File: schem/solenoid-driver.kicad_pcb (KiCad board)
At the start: 2 copper layers, 45.2 x 21.2 mm, 21 parts, among them P1 CONN_3X2, P3 CONN_2, P4 Chassis GND, U1 MIC2009A-1, U2 ULN2003, U3 MIC2250-2

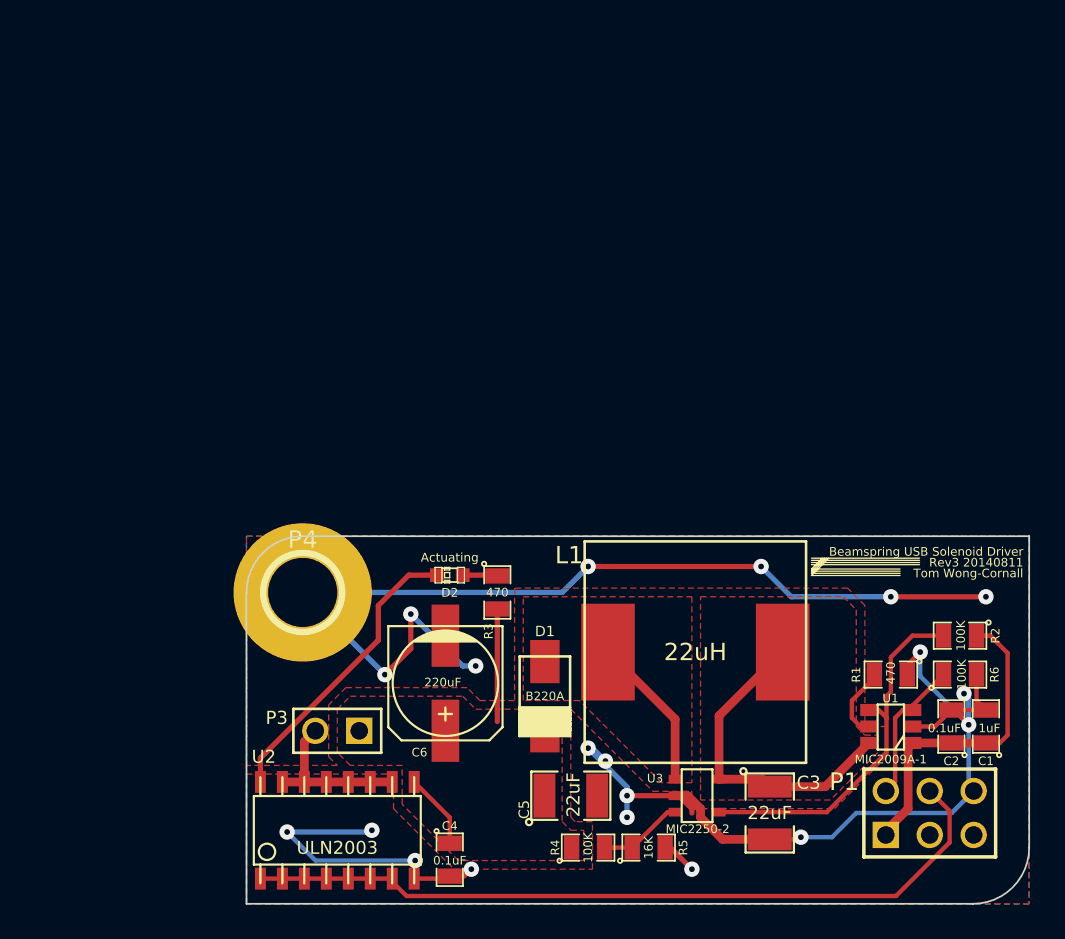
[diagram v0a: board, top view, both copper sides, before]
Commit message: Route the PCB
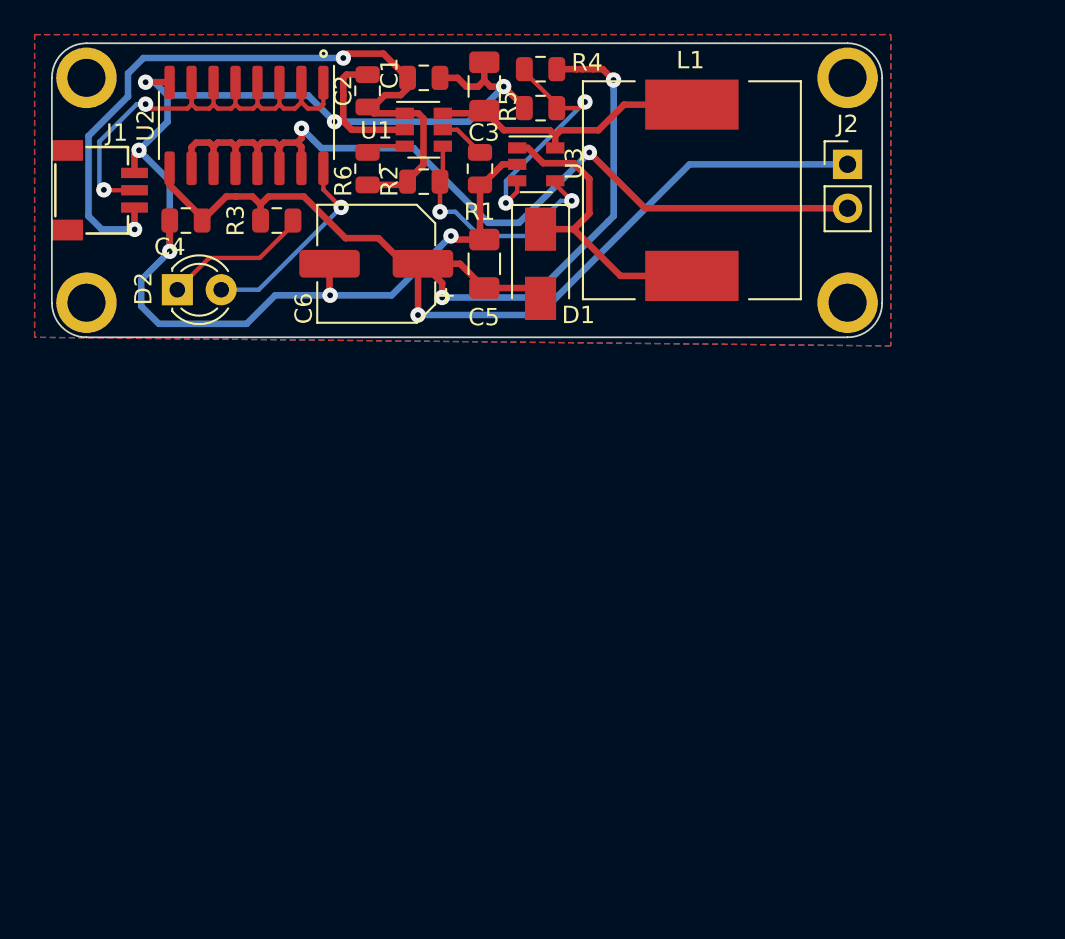
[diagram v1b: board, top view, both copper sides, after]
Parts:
- removed P1: CONN_3X2, pin_array_3x2
- removed P3: CONN_2, PIN_ARRAY_2X1
- removed P4: Chassis GND, 1pin
- added J1: Conn_01x03, random-keyboard-parts:JST-SR-3, F.Cu at (164.0, 117.5)
- added J2: SOLENOID, Connector_PinHeader_2.54mm:PinHeader_1x02_P2.54mm_Vertical, F.Cu at (210.0, 116.0)
- added MH1: Conn_01x01, random-keyboard-parts:Generic-Mounthole, F.Cu at (166.0, 111.0)
- added MH2: Conn_01x01, random-keyboard-parts:Generic-Mounthole, F.Cu at (166.0, 124.0)
- added MH3: Conn_01x01, random-keyboard-parts:Generic-Mounthole, F.Cu at (210.0, 111.0)
- added MH4: Conn_01x01, random-keyboard-parts:Generic-Mounthole, F.Cu at (210.0, 124.0)
- C1, C2, C4: footprint SM0805 -> Capacitor_SMD:C_0805_2012Metric
- C3, C5: footprint SM1210 -> Capacitor_SMD:C_1206_3216Metric
- C6: footprint c_elec_6.3x7.7 -> Capacitor_SMD:CP_Elec_6.3x7.7
- D1: footprint DO214AC_SMA -> Diode_SMD:D_SMA
- D2: footprint LED-0603 -> LED_THT:LED_D3.0mm
- L1: footprint INDUCTOR_12.8x12.8 -> Inductor_SMD:L_12x12mm_H6mm
- R1, R2, R3, R4, R5, R6: footprint SM0805 -> Resistor_SMD:R_0805_2012Metric
- U1: footprint SOT23_6 -> Package_TO_SOT_SMD:SOT-23-6
- U2: footprint so-16 -> Package_SO:SOIC-16_3.9x9.9mm_P1.27mm
- U3: footprint SOT23-5 -> Package_TO_SOT_SMD:SOT-23-5
- moved C2 49.9 mm to (182.2, 111.8)
- moved C1 49.6 mm to (185.5, 111.0), turned to 0 degrees
- moved C3 45.1 mm to (189.0, 111.5), turned to 90 degrees
- moved R4 45.1 mm to (192.2, 110.5), turned to 180 degrees
- moved R6 45.0 mm to (182.2, 116.2), turned to 270 degrees
- moved U1 43.8 mm to (185.5, 114.0), turned to 0 degrees
- moved R5 43.2 mm to (192.2, 112.8), turned to 180 degrees
- moved U2 41.1 mm to (175.2, 113.8), turned to 270 degrees
- moved R2 40.6 mm to (185.5, 117.0), turned to 0 degrees
- moved C4 40.0 mm to (171.8, 119.2), turned to 180 degrees
- moved R1 37.7 mm to (188.8, 116.2), turned to 90 degrees
- moved U3 37.7 mm to (192.0, 116.0), turned to 0 degrees
- moved C5 31.2 mm to (189.0, 121.8), turned to 90 degrees
- moved L1 26.7 mm to (201.0, 117.5), turned to 270 degrees
- moved D1 25.0 mm to (192.2, 121.8)
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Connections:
- net N-000005 renamed SIGNAL
- R6 pad 2: GND -> +5V
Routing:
- net +9V: track 10.9 -> 84.9 mm, vias 0 -> 3
- net Net-(J2-Pad2): track 9.57 -> 52.5 mm, vias 0 -> 2
- net GND: track 127.8 -> 86.9 mm, vias 20 -> 7
- net +5V: track 18.6 -> 44.0 mm, vias 0 -> 2
- net SIGNAL: track 45.1 -> 28.7 mm, vias 0 -> 2
- net Net-(R4-Pad2): track 4.93 -> 14.1 mm, vias 0 -> 2
- net /SW: track 8.95 -> 18.1 mm
- net Net-(R2-Pad2): track 21.5 -> 14.5 mm, vias 0 -> 2
- net Net-(D2-Pad1): track 2.02 -> 8.86 mm
- net Net-(R6-Pad1): track 8.44 -> 2.30 mm
- net Net-(D2-Pad2): track 17.1 -> 11.6 mm, vias 0 -> 1
- net /+5V_Gated: track 18.8 -> 16.5 mm
- net Net-(R1-Pad2): track 4.22 -> 2.69 mm
- removed copper zone on F.Cu, net +9V
- removed copper zone on F.Cu, net /+5V_Gated
- removed copper zone on F.Cu, net /SW
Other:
- board size 45.2 x 21.2 mm -> 48 x 17 mm
- net class Power added: clearance 0.2032, trace_width 0.381, via_dia 0.889, via_drill 0.3302
- board text removed: "Beamspring USB Solenoid Driver"
- board text removed: "Rev3 20140811"
- board text removed: "Tom Wong-Cornall"

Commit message: Finalize PCB
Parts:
- removed C4: 0.1uF, Capacitor_SMD:C_0805_2012Metric
- removed U2: ULN2003, Package_SO:SOIC-16_3.9x9.9mm_P1.27mm
- added C7: 10uF, Capacitor_SMD:C_0805_2012Metric, F.Cu at (180.0, 116.2)
- added Q1: AO3400, Package_TO_SOT_SMD:SOT-23, F.Cu at (179.0, 111.8)
- added R7: 100, Resistor_SMD:R_0805_2012Metric, F.Cu at (177.8, 116.2)
- D2: value Actuating -> RB060T; footprint LED_THT:LED_D3.0mm -> Diode_SMD:D_SOD-123
- R3: value 470 -> 100K
- R6: value 100K -> 270k
- moved D2 15.1 mm to (186.2, 121.8), turned to 270 degrees
- moved R3 7.60 mm to (175.8, 111.8), turned to 270 degrees
- moved J1 6.00 mm to (170.0, 117.5)
- moved MH1 6.00 mm to (172.0, 111.0)
- moved MH2 6.00 mm to (172.0, 124.0)
- moved C6 2.75 mm to (180.0, 121.8)
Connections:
- net Net-(R6-Pad1) renamed ENABLE
- D2 pad 1: Net-(D2-Pad1) -> +9V
- J2 pad 2: Net-(J2-Pad2) -> Net-(D2-Pad2)
- R3 pad 1: Net-(D2-Pad1) -> GND
- R3 pad 2: +9V -> Net-(Q1-Pad1)
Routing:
- net Net-(J2-Pad2): track 52.5 -> 0.00 mm, vias 2 -> 0
- net Net-(D2-Pad2): track 11.6 -> 49.6 mm, vias 1 -> 2
- net +9V: track 84.9 -> 55.4 mm, vias 3 -> 2
- net SIGNAL: track 28.7 -> 3.10 mm, vias 2 -> 0
- net GND: track 86.9 -> 76.7 mm, vias 7 -> 6
- net +5V: track 44.0 -> 33.9 mm
- net Net-(D2-Pad1): track 8.86 -> 0.00 mm
- net Net-(Q1-Pad1): track 0.00 -> 5.78 mm
- net ENABLE: track 2.30 -> 4.55 mm
- removed copper zone on B.Cu, net GND
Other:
- board size 48 x 17 mm -> 42 x 17 mm
- board text added: "UNIFIED-S9"
- board text added: "Unified Daughterboard S9 9-Volt Solenoid Controller Original circuit by xwhatsit, licensed GPLv3 Connect solenoid to J2"
